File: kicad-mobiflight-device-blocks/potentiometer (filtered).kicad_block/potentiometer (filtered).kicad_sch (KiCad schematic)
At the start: 1 part

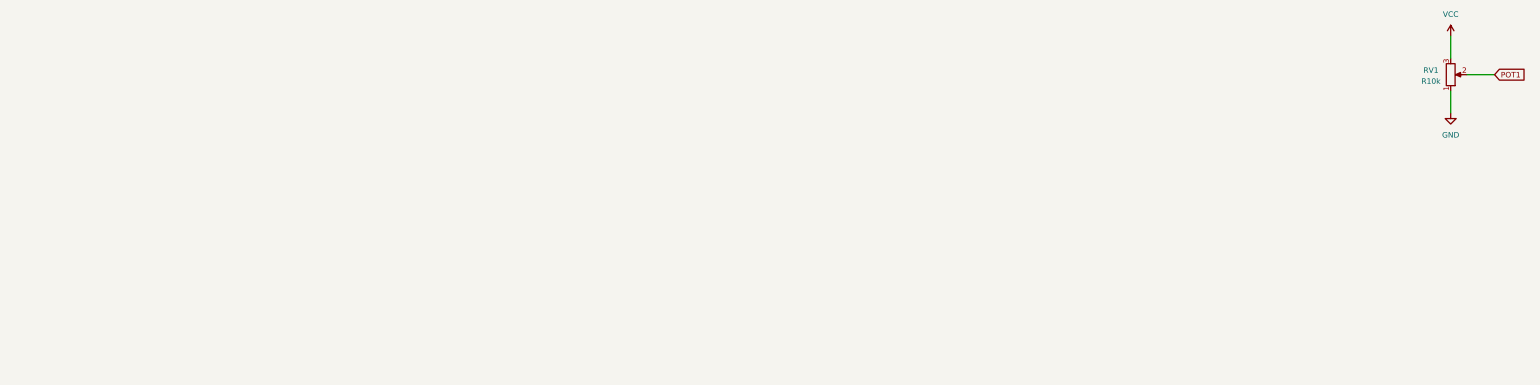
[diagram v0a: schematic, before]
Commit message: added plain potentiometer block, reworked layout of potentiometer blocks (signal goes to right, vcc up, gnd bottom) (#1)
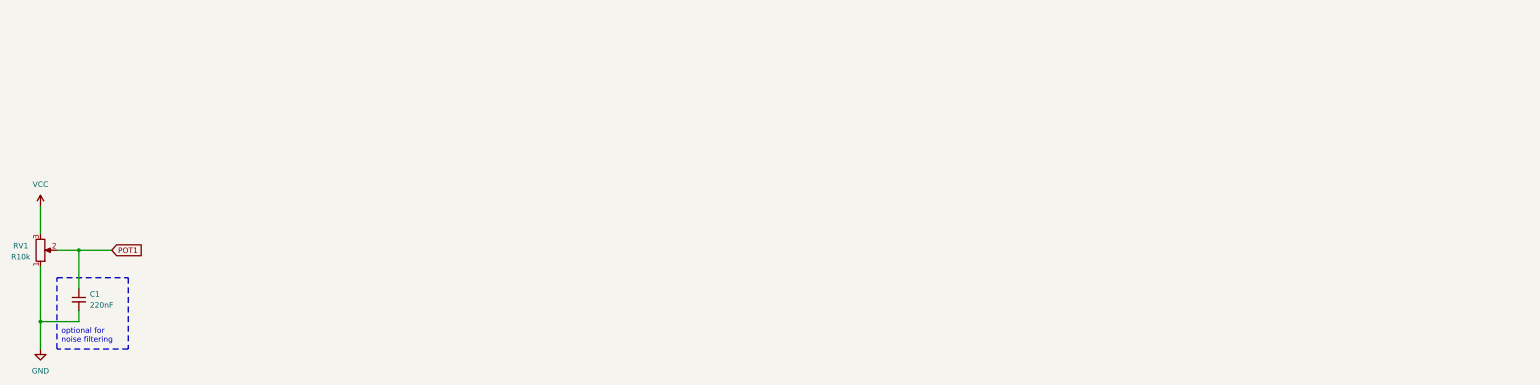
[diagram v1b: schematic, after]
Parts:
- added C1: 220nF, Capacitor_THT:C_Disc_D7.0mm_W2.5mm_P5.00mm, symbol Device:C_Small
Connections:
- net GND: now also C1.2
- net POT1: now also C1.1
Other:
- note added: "optional for noise filtering"
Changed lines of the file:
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@@
 	(generator_version "10.0")
 	(paper "A4")
-	(wire
-		(pts
-			(xy 356.87 73.66) (xy 356.87 78.74)
-		)
-		(stroke
-			(width 0)
-			(type default)
-		)
-	)
-	(wire
-		(pts
-			(xy 360.68 69.85) (xy 367.03 69.85)
-		)
-		(stroke
-			(width 0)
-			(type default)
-		)
-	)
-	(wire
-		(pts
-			(xy 356.87 60.96) (xy 356.87 66.04)
+	(rectangle
+		(start 34.29 116.84)
+		(end 50.8 133.35)
+		(stroke
+			(width 0)
+			(type dash)
+		)
+		(fill
+			(type none)
+		)
+	)
+	(text "optional for\nnoise filtering"
+		(exclude_from_sim no)
+		(at 35.306 130.302 0)
+		(effects
+			(font
+				(size 1.27 1.27)
+			)
+			(justify left)
+		)
+	)
+	(junction
+		(at 30.48 127)
+		(diameter 0)
+		(color 0 0 0 0)
+	)
+	(junction
+		(at 39.37 110.49)
+		(diameter 0)
+		(color 0 0 0 0)
+	)
+	(wire
+		(pts
+			(xy 39.37 110.49) (xy 46.99 110.49)
+		)
+		(stroke
+			(width 0)
+			(type default)
+		)
+	)
+	(wire
+		(pts
+			(xy 30.48 114.3) (xy 30.48 127)
+		)
+		(stroke
+			(width 0)
+			(type default)
+		)
+	)
+	(wire
+		(pts
+			(xy 39.37 110.49) (xy 39.37 119.38)
+		)
+		(stroke
+			(width 0)
+			(type default)
+		)
+	)
+	(wire
+		(pts
+			(xy 39.37 124.46) (xy 39.37 127)
+		)
+		(stroke
+			(width 0)
+			(type default)
+		)
+	)
+	(wire
+		(pts
+			(xy 39.37 127) (xy 30.48 127)
+		)
+		(stroke
+			(width 0)
+			(type default)
+		)
+	)
+	(wire
+		(pts
+			(xy 30.48 100.33) (xy 30.48 106.68)
+		)
+		(stroke
+			(width 0)
+			(type default)
+		)
+	)
+	(wire
+		(pts
+			(xy 34.29 110.49) (xy 39.37 110.49)
+		)
+		(stroke
+			(width 0)
+			(type default)
+		)
+	)
+	(wire
+		(pts
+			(xy 30.48 133.35) (xy 30.48 127)
 		)
 		(stroke
@@
 	(global_label "POT1"
 		(shape input)
-		(at 367.03 69.85 0)
+		(at 46.99 110.49 0)
 		(fields_autoplaced yes)
 		(effects
@@
 		)
 		(property "Intersheetrefs" "${INTERSHEET_REFS}"
-			(at 374.7928 69.85 0)
+			(at 54.7528 110.49 0)
 			(hide yes)
 			(show_name no)
@@
 				)
 				(justify left)
+			)
+		)
+	)
+	(symbol
+		(lib_id "power:GND")
+		(at 30.48 133.35 0)
+		(unit 1)
+		(body_style 1)
+		(exclude_from_sim no)
+		(in_bom yes)
+		(on_board yes)
+		(in_pos_files yes)
+		(dnp no)
+		(fields_autoplaced yes)
+		(property "Reference" "#PWR021"
+			(at 30.48 139.7 0)
+			(hide yes)
+			(show_name no)
+			(do_not_autoplace no)
+			(effects
+				(font
+					(size 1.27 1.27)
+				)
+			)
+		)
+		(property "Value" "GND"
+			(at 30.48 138.43 0)
+			(show_name no)
+			(do_not_autoplace no)
+			(effects
+				(font
+					(size 1.27 1.27)
+				)
+			)
+		)
+		(property "Footprint" ""
+			(at 30.48 133.35 0)
+			(hide yes)
+			(show_name no)
+			(do_not_autoplace no)
+			(effects
+				(font
+					(size 1.27 1.27)
+				)
+			)
+		)
+		(property "Datasheet" ""
+			(at 30.48 133.35 0)
+			(hide yes)
+			(show_name no)
+			(do_not_autoplace no)
+			(effects
+				(font
+					(size 1.27 1.27)
+				)
+			)
+		)
+		(property "Description" "Power symbol creates a global label with name \"GND\" , ground"
+			(at 30.48 133.35 0)
+			(hide yes)
+			(show_name no)
+			(do_not_autoplace no)
+			(effects
+				(font
+					(size 1.27 1.27)
+				)
+			)
+		)
+		(pin "1"
+		)
+		(instances
+			(project "panel-pcb-kicad"
+				(path "/6be401a8-e515-4f8d-8c23-da9295db45d6"
+					(reference "#PWR021")
+					(unit 1)
+				)
 			)
 		)
@@
 	(symbol
 		(lib_id "power:VCC")
-		(at 356.87 60.96 0)
+		(at 30.48 100.33 0)
 		(unit 1)
 		(body_style 1)
@@
 		(fields_autoplaced yes)
 		(property "Reference" "#PWR022"
-			(at 356.87 64.77 0)
+			(at 30.48 104.14 0)
 			(hide yes)
 			(show_name no)
@@
 		)
 		(property "Value" "VCC"
-			(at 356.87 55.88 0)
+			(at 30.48 95.25 0)
 			(show_name no)
 			(do_not_autoplace no)
@@
 		)
 		(property "Footprint" ""
-			(at 356.87 60.96 0)
+			(at 30.48 100.33 0)
 			(hide yes)
 			(show_name no)
@@
 		)
 		(property "Datasheet" ""
-			(at 356.87 60.96 0)
+			(at 30.48 100.33 0)
 			(hide yes)
 			(show_name no)
@@
 		)
 		(property "Description" "Power symbol creates a global label with name \"VCC\""
-			(at 356.87 60.96 0)
+			(at 30.48 100.33 0)
 			(hide yes)
 			(show_name no)
@@
 	)
 	(symbol
-		(lib_id "power:GND")
-		(at 356.87 78.74 0)
-		(unit 1)
-		(body_style 1)
-		(exclude_from_sim no)
-		(in_bom yes)
-		(on_board yes)
-		(in_pos_files yes)
-		(dnp no)
-		(fields_autoplaced yes)
-		(property "Reference" "#PWR021"
-			(at 356.87 85.09 0)
-			(hide yes)
-			(show_name no)
-			(do_not_autoplace no)
-			(effects
-				(font
-					(size 1.27 1.27)
-				)
-			)
-		)
-		(property "Value" "GND"
-			(at 356.87 83.82 0)
-			(show_name no)
-			(do_not_autoplace no)
-			(effects
-				(font
-					(size 1.27 1.27)
-				)
-			)
-		)
-		(property "Footprint" ""
-			(at 356.87 78.74 0)
-			(hide yes)
-			(show_name no)
-			(do_not_autoplace no)
-			(effects
-				(font
-					(size 1.27 1.27)
-				)
-			)
-		)
-		(property "Datasheet" ""
-			(at 356.87 78.74 0)
-			(hide yes)
-			(show_name no)
-			(do_not_autoplace no)
-			(effects
-				(font
-					(size 1.27 1.27)
-				)
-			)
-		)
-		(property "Description" "Power symbol creates a global label with name \"GND\" , ground"
-			(at 356.87 78.74 0)
-			(hide yes)
-			(show_name no)
-			(do_not_autoplace no)
-			(effects
-				(font
-					(size 1.27 1.27)
-				)
-			)
-		)
-		(pin "1"
-		)
-		(instances
-			(project "panel-pcb-kicad"
-				(path "/6be401a8-e515-4f8d-8c23-da9295db45d6"
-					(reference "#PWR021")
-					(unit 1)
-				)
-			)
-		)
-	)
-	(symbol
 		(lib_id "Device:R_Potentiometer")
-		(at 356.87 69.85 0)
+		(at 30.48 110.49 0)
 		(mirror x)
 		(unit 1)
@@
 		(dnp no)
 		(property "Reference" "RV1"
-			(at 352.298 68.834 0)
+			(at 25.908 109.474 0)
 			(show_name no)
 			(do_not_autoplace no)
@@
 		)
 		(property "Value" "R10k"
-			(at 352.298 71.374 0)
+			(at 25.908 112.014 0)
 			(show_name no)
 			(do_not_autoplace no)
@@
 		)
 		(property "Footprint" "MobiFlight Devices:Potentiometer_Alps_RK09K_Single_Vertical"
-			(at 356.87 69.85 0)
+			(at 30.48 110.49 0)
 			(hide yes)
 			(show_name no)
@@
 		)
 		(property "Datasheet" ""
-			(at 356.87 69.85 0)
+			(at 30.48 110.49 0)
 			(hide yes)
 			(show_name no)
@@
 		)
 		(property "Description" "Potentiometer"
-			(at 356.87 69.85 0)
+			(at 30.48 110.49 0)
 			(hide yes)
 			(show_name no)
@@
 					(unit 1)
 				)
+			)
+		)
+	)
+	(symbol
+		(lib_id "Device:C_Small")
+		(at 39.37 121.92 0)
+		(unit 1)
+		(body_style 1)
+		(exclude_from_sim no)
+		(in_bom yes)
+		(on_board yes)
+		(in_pos_files yes)
+		(dnp no)
+		(fields_autoplaced yes)
+		(property "Reference" "C1"
+			(at 41.91 120.6562 0)
+			(show_name no)
+			(do_not_autoplace no)
+			(effects
+				(font
+					(size 1.27 1.27)
+				)
+				(justify left)
+			)
+		)
+		(property "Value" "220nF"
+			(at 41.91 123.1962 0)
+			(show_name no)
+			(do_not_autoplace no)
+			(effects
+				(font
+					(size 1.27 1.27)
+				)
+				(justify left)
+			)
+		)
+		(property "Footprint" "Capacitor_THT:C_Disc_D7.0mm_W2.5mm_P5.00mm"
+			(at 39.37 121.92 0)
+			(hide yes)
+			(show_name no)
+			(do_not_autoplace no)
+			(effects
+				(font
+					(size 1.27 1.27)
+				)
+			)
+		)
+		(property "Datasheet" ""
+			(at 39.37 121.92 0)
+			(hide yes)
+			(show_name no)
+			(do_not_autoplace no)
+			(effects
+				(font
+					(size 1.27 1.27)
+				)
+			)
+		)
+		(property "Description" "Unpolarized capacitor, small symbol"
+			(at 39.37 121.92 0)
+			(hide yes)
+			(show_name no)
+			(do_not_autoplace no)
+			(effects
+				(font
+					(size 1.27 1.27)
+				)
+			)
+		)
+		(pin "1"
+		)
+		(pin "2"
+		)
+		(instances
+			(project "panel-pcb-kicad"
+				(path "/6be401a8-e515-4f8d-8c23-da9295db45d6"
+					(reference "C1")
+					(unit 1)
+				)
